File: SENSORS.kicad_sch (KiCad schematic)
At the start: 25 parts, among them J8 Conn_01x04, J9 Conn_01x04, U5 BMI088, U6 LSM6DSV16X, U7 ICM-45686, U8 BMP581, U9 DPS368XTSA1

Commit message: change package
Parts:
- U7: CAD Symbol Verification Pinout cross-checked against TDK DS-000577 Rev 1.0; Ultra L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 -> (none); DigiKey Description IMU ACCEL GYRO 6 AXIS -> (none); DigiKey Detailed Description Accelerometer, Gyroscope, 6 Axis Sensor I2C, I3C, SPI Output -> (none); DigiKey Digi-Reel Part Number 1428-ICM-45686DKR-ND -> (none); DigiKey ECCN EAR99 -> (none); DigiKey EDA Models URL https://www.digikey.com/en/models/24374985 -> (none); DigiKey HTSUS 8542.39.0070 -> (none); DigiKey MSL 1 (Unlimited) -> (none); DigiKey Mounting Surface Mount -> (none); DigiKey Package Case 14-VFLGA -> (none); DigiKey Part Status Active -> (none); DigiKey Price Qty 1 CT -> (none); DigiKey REACH Not Affected -> (none); DigiKey RoHS RoHS 3 Compliant -> (none); DigiKey Series SmartMotion -> (none); DigiKey Specs 6-axis accel + gyro, I2C/I3C/SPI, LGA-14 3.0x2.5 mm -> (none); DigiKey Standard Lead Time 45 Weeks -> (none); DigiKey Status Active; no stock at audit -> (none); DigiKey Stock 0 -> (none); DigiKey Supplier Device Package 14-LGA (2.5x3) -> (none); DigiKey TR Part Number 1428-ICM-45686TR-ND -> (none); DigiKey Unit Price EUR 4.60 -> (none); Footprint Audit Package dimensions confirmed from DigiKey/TDK; current foot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 -> (none); LCSC C22459454 -> (none); LCSC Part C22459454 -> (none); Library Audit Project-local H743_Ardupilot symbol; pinout from TDK datash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 -> (none); Price Checked 2026-09-25 -> (none)
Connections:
- net +3V3_MCU: now also U7.5 (VDDIO)
- net +3V3_SENS: now also U7.8 (VDD)
- net GND: now also U7.6 (GND)
- net SPI1.CS: now also U7.12 (CS)
- net SPI1.MISO: now also U7.1 (SDO/AD0)
- net SPI1.MOSI: now also U7.14 (SDI/SDIO/SDA)
- net SPI1.SCLK: now also U7.13 (SCLK/SCL)
- net at R28.2: now also U7.4 (INT1)
- net at R29.2: now also U7.9 (INT2/FSYNC/CLKIN)
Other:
- moved on the sheet: R28, R29

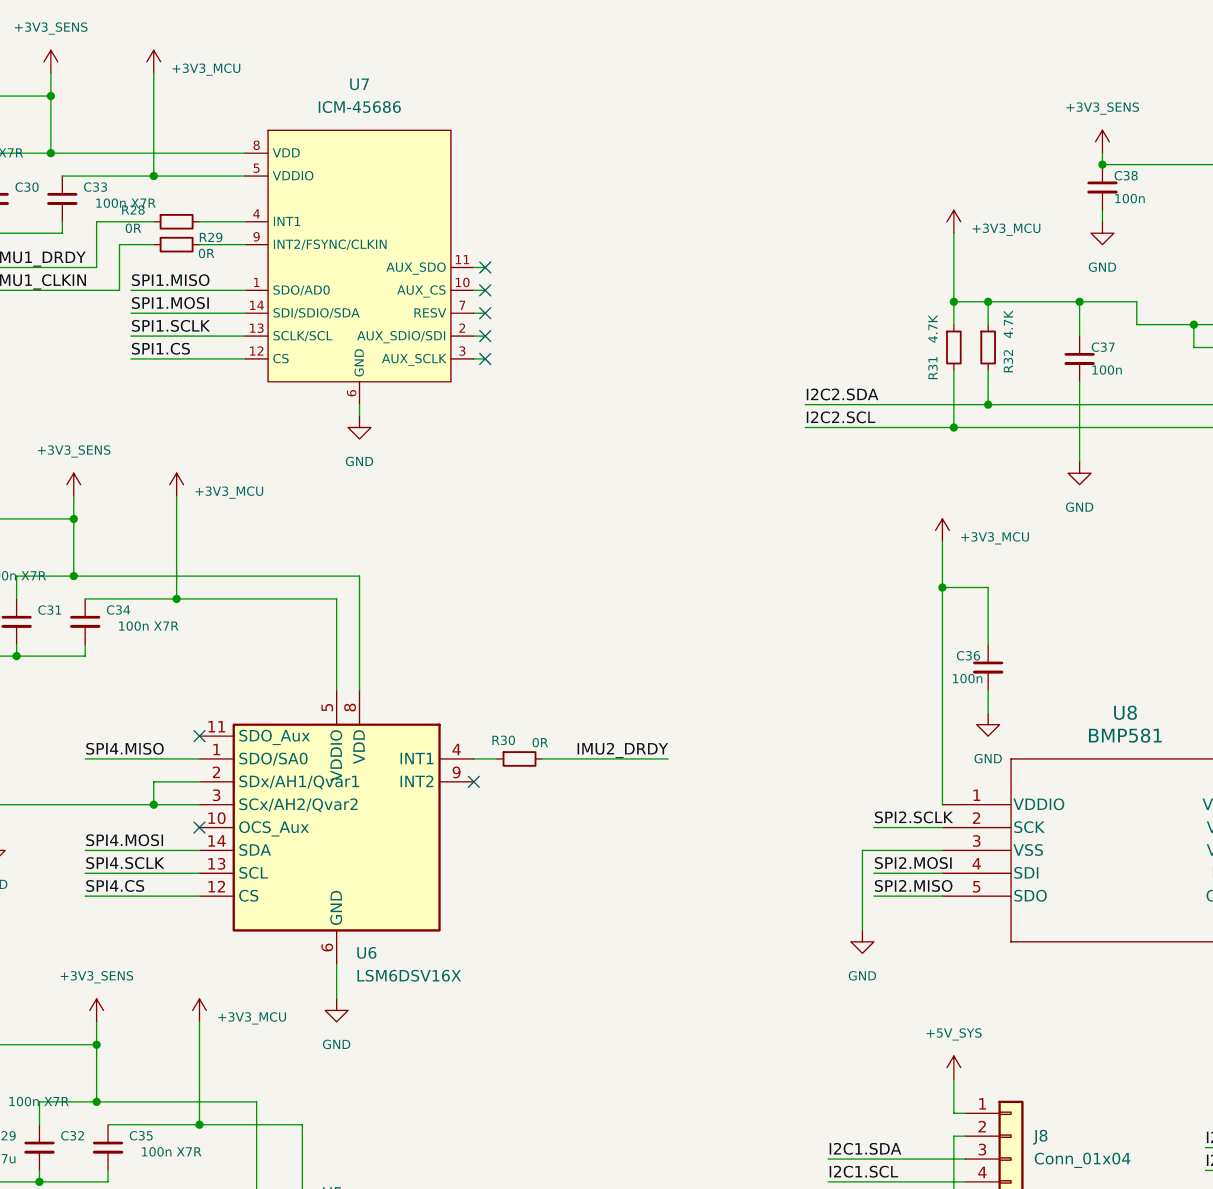
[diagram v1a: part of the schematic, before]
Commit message: move all sensor VDDIO rails to 3V3_SENS
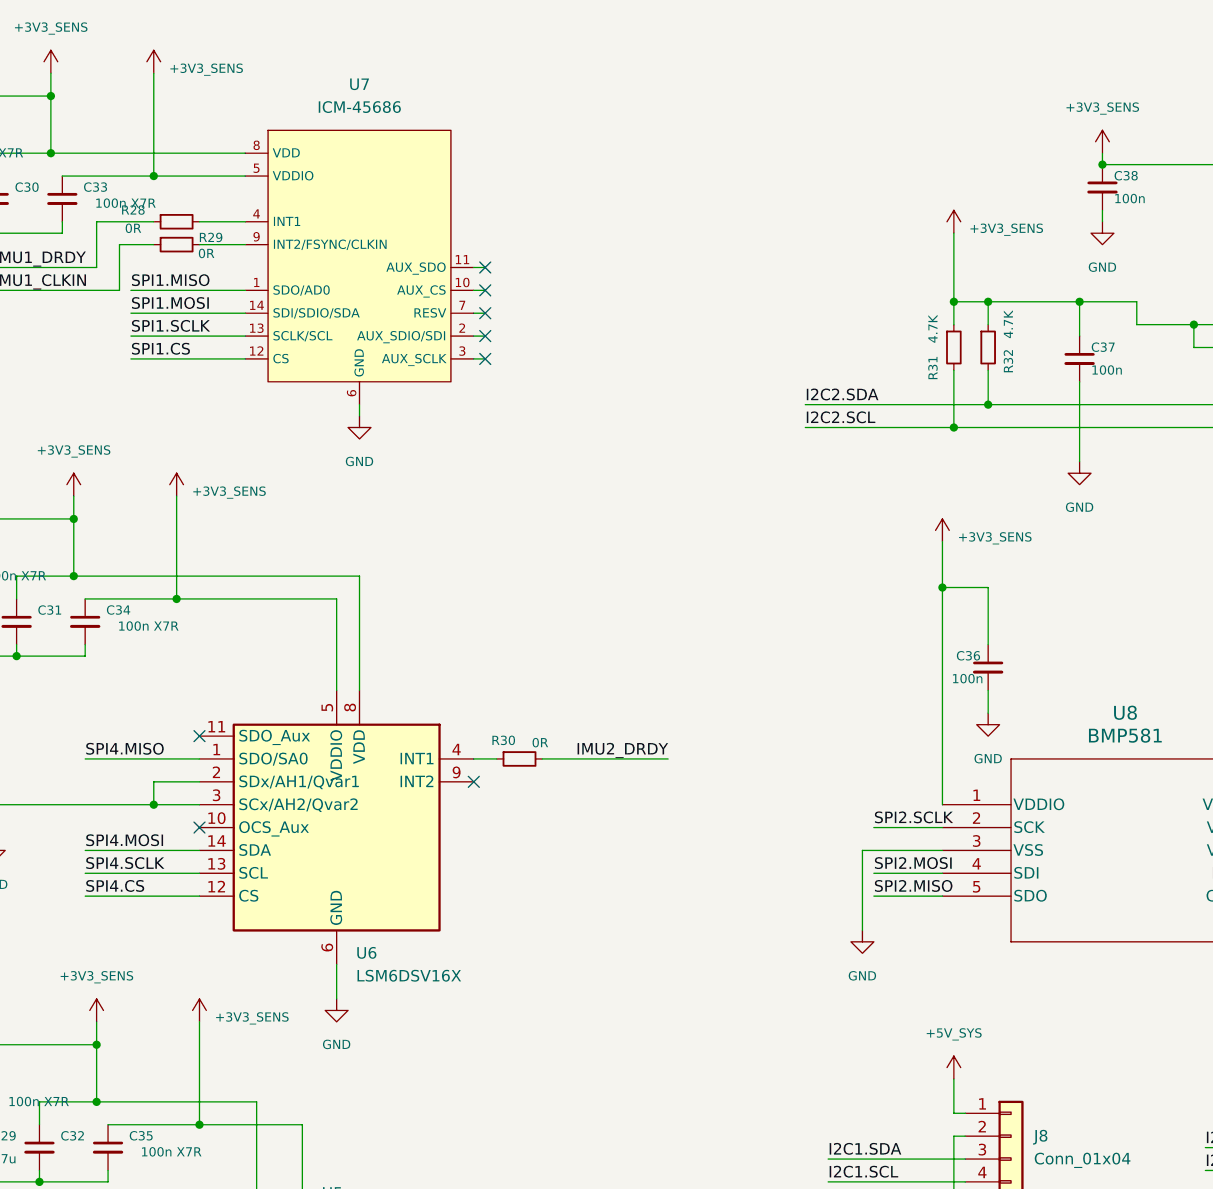
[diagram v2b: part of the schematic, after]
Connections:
- net +3V3_MCU is gone; now on net +3V3_SENS: C33.1, C34.1, C35.1, C36.1, C37.1, R31.1, R32.1, U5.11 (VDDIO), U6.5 (VDDIO), U7.5 (VDDIO), U8.1 (VDDIO), U9.2 (CSB), U9.6 (VDDIO)
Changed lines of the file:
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@@
 			)
 		)
-		(property "Value" "+3V3_MCU"
+		(property "Value" "+3V3_SENS"
 			(at 129.032 126.492 0)
 			(show_name no)
@@
 			)
 		)
-		(property "Value" "+3V3_MCU"
+		(property "Value" "+3V3_SENS"
 			(at 211.582 73.152 0)
 			(show_name no)
@@
 			)
 		)
-		(property "Value" "+3V3_MCU"
+		(property "Value" "+3V3_SENS"
 			(at 126.492 68.072 0)
 			(show_name no)
@@
 			)
 		)
-		(property "Value" "+3V3_MCU"
+		(property "Value" "+3V3_SENS"
 			(at 212.852 38.862 0)
 			(show_name no)
@@
 			)
 		)
-		(property "Value" "+3V3_MCU"
+		(property "Value" "+3V3_SENS"
 			(at 123.952 21.082 0)
 			(show_name no)

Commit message: restore sensor VDDIO rails to 3V3_MCU
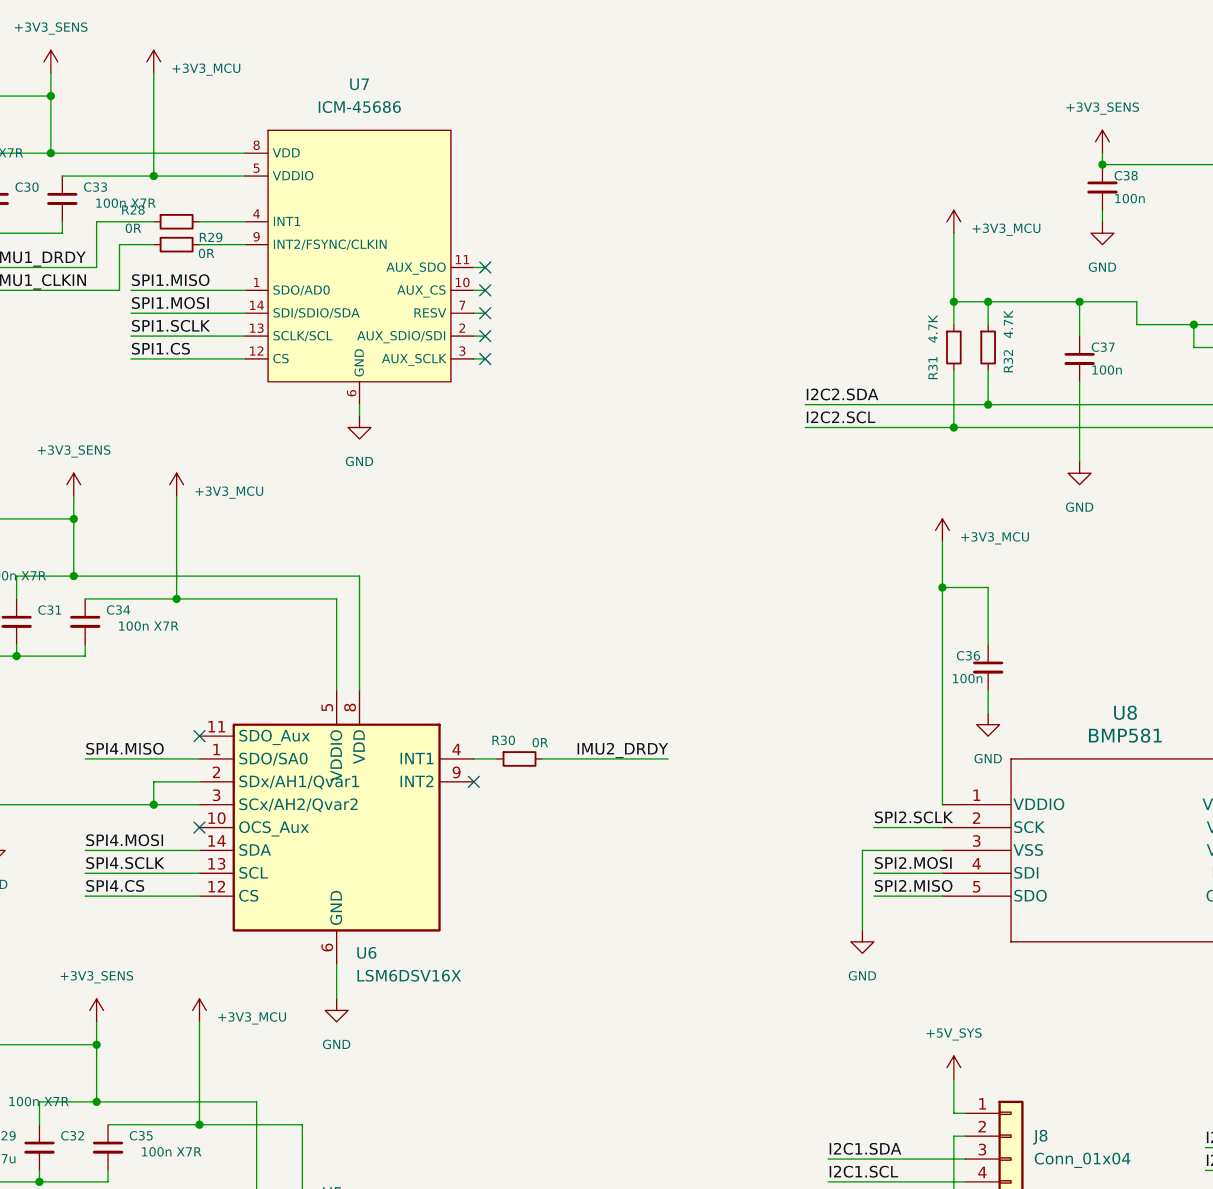
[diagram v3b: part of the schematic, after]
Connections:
- net +3V3_SENS: no longer C33.1, C34.1, C35.1, C36.1, C37.1, R31.1, R32.1, U5.11 (VDDIO), U6.5 (VDDIO), U7.5 (VDDIO), U8.1 (VDDIO), U9.2 (CSB), U9.6 (VDDIO)
- new net +3V3_MCU: C33.1, C34.1, C35.1, C36.1, C37.1, R31.1, R32.1, U5.11 (VDDIO), U6.5 (VDDIO), U7.5 (VDDIO), U8.1 (VDDIO), U9.2 (CSB), U9.6 (VDDIO)
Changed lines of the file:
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@@
 			)
 		)
-		(property "Value" "+3V3_SENS"
+		(property "Value" "+3V3_MCU"
 			(at 129.032 126.492 0)
 			(show_name no)
@@
 			)
 		)
-		(property "Value" "+3V3_SENS"
+		(property "Value" "+3V3_MCU"
 			(at 211.582 73.152 0)
 			(show_name no)
@@
 			)
 		)
-		(property "Value" "+3V3_SENS"
+		(property "Value" "+3V3_MCU"
 			(at 126.492 68.072 0)
 			(show_name no)
@@
 			)
 		)
-		(property "Value" "+3V3_SENS"
+		(property "Value" "+3V3_MCU"
 			(at 212.852 38.862 0)
 			(show_name no)
@@
 			)
 		)
-		(property "Value" "+3V3_SENS"
+		(property "Value" "+3V3_MCU"
 			(at 123.952 21.082 0)
 			(show_name no)

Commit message: assign Matek-style solder pad footprints in SENSORS.kicad_sch
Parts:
- J8, J9: footprint (none) -> H743_Custom:SolderPadArray_1x04_P2.54mm_1x1mm; DigiKey Status TBD: connector not physically selected -> PCB feature / no purchased component; Footprint Audit BLOCKING: no footprint assigned -> OK: 4 square SMD pads 1.00x1.00 mm, P2.54 mm, no holes, no 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; Library Audit Generic KiCad connector -> Project-local H743_Custom footprint; Package TBD -> Solder pad array 1x4, P2.54 mm, 1.00x1.00 mm SMD
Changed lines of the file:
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@@
 			)
 		)
-		(property "Footprint" ""
+		(property "Footprint" "H743_Custom:SolderPadArray_1x04_P2.54mm_1x1mm"
 			(at 255.27 138.43 0)
 			(hide yes)
@@
 			)
 		)
-		(property "DigiKey Status" "TBD: connector not physically selected"
+		(property "DigiKey Status" "PCB feature / no purchased component"
 			(at 257.81 138.4299 0)
 			(hide yes)
@@
 			)
 		)
-		(property "Package" "TBD"
+		(property "Package" "Solder pad array 1x4, P2.54 mm, 1.00x1.00 mm SMD"
 			(at 257.81 138.4299 0)
 			(hide yes)
@@
 			)
 		)
-		(property "Footprint Audit" "BLOCKING: no footprint assigned"
+		(property "Footprint Audit" "OK: 4 square SMD pads 1.00x1.00 mm, P2.54 mm, no holes, no paste"
 			(at 257.81 138.4299 0)
 			(hide yes)
@@
 			)
 		)
-		(property "Library Audit" "Generic KiCad connector"
+		(property "Library Audit" "Project-local H743_Custom footprint"
 			(at 257.81 138.4299 0)
 			(hide yes)
@@
 			)
 		)
-		(property "Footprint" ""
+		(property "Footprint" "H743_Custom:SolderPadArray_1x04_P2.54mm_1x1mm"
 			(at 213.36 139.7 0)
 			(hide yes)
@@
 			)
 		)
-		(property "DigiKey Status" "TBD: connector not physically selected"
+		(property "DigiKey Status" "PCB feature / no purchased component"
 			(at 215.9 139.6999 0)
 			(hide yes)
@@
 			)
 		)
-		(property "Package" "TBD"
+		(property "Package" "Solder pad array 1x4, P2.54 mm, 1.00x1.00 mm SMD"
 			(at 215.9 139.6999 0)
 			(hide yes)
@@
 			)
 		)
-		(property "Footprint Audit" "BLOCKING: no footprint assigned"
+		(property "Footprint Audit" "OK: 4 square SMD pads 1.00x1.00 mm, P2.54 mm, no holes, no paste"
 			(at 215.9 139.6999 0)
 			(hide yes)
@@
 			)
 		)
-		(property "Library Audit" "Generic KiCad connector"
+		(property "Library Audit" "Project-local H743_Custom footprint"
 			(at 215.9 139.6999 0)
 			(hide yes)

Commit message: update
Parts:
- renumbered C27 to C44, C28 to C45, C29 to C46, C30 to C47, C31 to C48, C32 to C49, C33 to C50, C34 to C51, C35 to C52, C36 to C53, C37 to C54, C38 to C55, C39 to C56, R28 to R34, R29 to R35, R30 to R36, R31 to R37, R32 to R38, U6 to U10, U7 to U11, U8 to U12, U9 to U13, U5 to U9

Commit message: update pcb
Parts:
- J8: value Conn_01x04 -> I2C1
- J9: value Conn_01x04 -> I2C_2
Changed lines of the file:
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@@
 			)
 		)
-		(property "Value" "Conn_01x04"
+		(property "Value" "I2C_2"
 			(at 257.81 140.9699 0)
 			(show_name no)
@@
 			)
 		)
-		(property "Value" "Conn_01x04"
+		(property "Value" "I2C1"
 			(at 215.9 142.2399 0)
 			(show_name no)

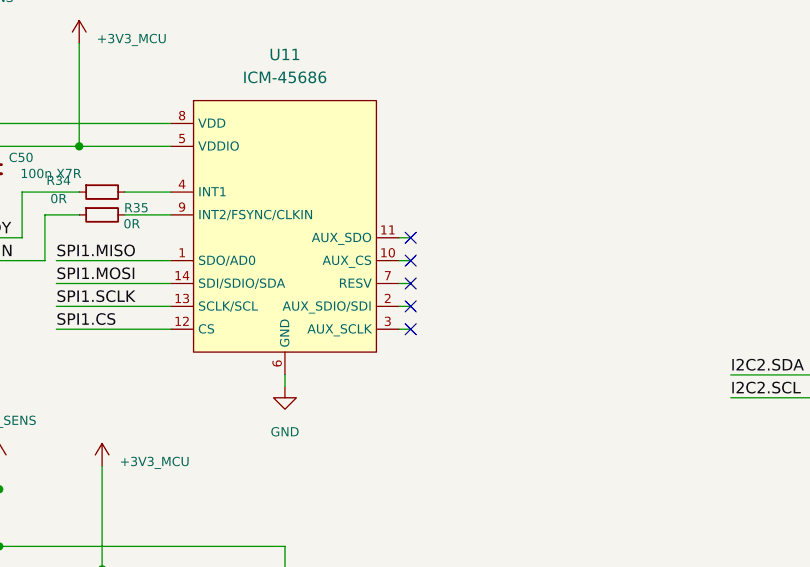
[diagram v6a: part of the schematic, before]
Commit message: Review component footprints, restore local libraries and reconcile PCB pads
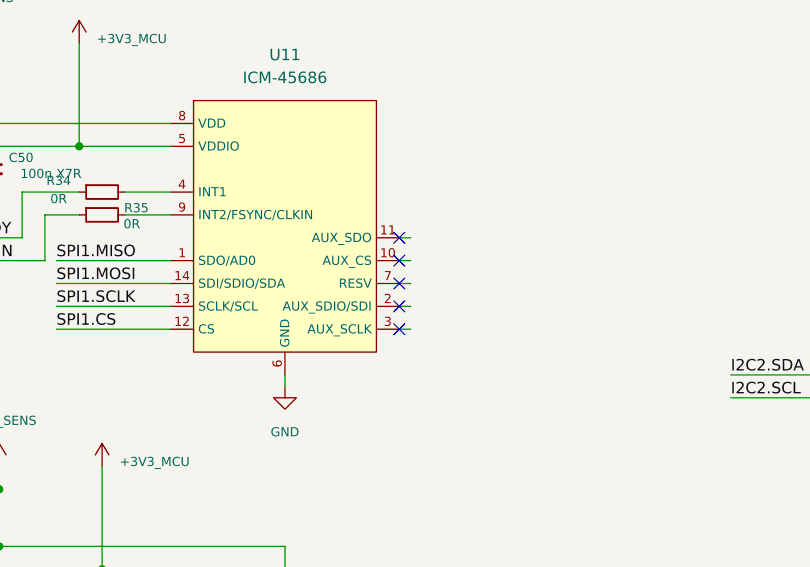
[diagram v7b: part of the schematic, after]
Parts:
- C44, C45, C46, C47, C48, C49, C50, C51, C52, C53, C54, C55, C56: symbol Device:C_Small -> FC01_Project:SENSORS__C_Small; Footprint Audit OK -> See verification/COMPONENTS.csv and verification/REPORT.md; Library Audit KiCad standard -> See verification/COMPONENTS.csv and verification/REPORT.md
- J8, J9: symbol Connector_Generic:Conn_01x04 -> FC01_Project:SENSORS__Conn_01x04; Footprint Audit OK: 4 square SMD pads 1.00x1.00 mm, P2.54 mm, no holes, no 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 -> See verification/COMPONENTS.csv and verification/REPORT.md; Library Audit Project-local H743_Custom footprint -> See verification/COMPONENTS.csv and verification/REPORT.md
- R34, R35, R36, R37, R38: symbol Device:R_Small -> FC01_Project:SENSORS__R_Small; Footprint Audit OK -> See verification/COMPONENTS.csv and verification/REPORT.md; Library Audit KiCad standard -> See verification/COMPONENTS.csv and verification/REPORT.md
- U10: symbol H743_Ardupilot:LSM6DSV16X -> FC01_Project:SENSORS__LSM6DSV16X; Footprint Audit OK: KiCad LGA-14 3x2.5 P0.5 -> See verification/COMPONENTS.csv and verification/REPORT.md; Library Audit Embedded H743_Ardupilot symbol + KiCad footprint -> See verification/COMPONENTS.csv and verification/REPORT.md
- U11: footprint EasyEDA:LGA-14_L3.0-W2.5-P0.50-TL -> H743_Custom:TDK_ICM45686_LGA14_3x2.5mm; symbol H743_Ardupilot:ICM-45686 -> FC01_Project:SENSORS__ICM-45686
- U12: symbol BMP581:BMP581 -> FC01_Project:SENSORS__BMP581; Footprint Audit OK: Bosch recommended land pattern corrected 2026-09-25 -> See verification/COMPONENTS.csv and verification/REPORT.md; Library Audit Project BMP581 symbol + H743_Custom footprint -> See verification/COMPONENTS.csv and verification/REPORT.md
- U13: footprint EasyEDA:LGA-8_L2.5-W2.0-P0.65-TR_DPS368 -> H743_Custom:Infineon_DPS368_PG-VLGA-8-2; symbol EasyEDA:DPS368XTSA1 -> FC01_Project:SENSORS__DPS368XTSA1_1; Footprint Audit OK by dimensions; final land-pattern overlay recommended -> See verification/COMPONENTS.csv and verification/REPORT.md; Library Audit EasyEDA external -> See verification/COMPONENTS.csv and verification/REPORT.md
- U9: symbol Sensor_Motion:BMI088 -> FC01_Project:SENSORS__BMI088; Footprint Audit OK: KiCad Bosch LGA-16 -> See verification/COMPONENTS.csv and verification/REPORT.md; Library Audit KiCad Sensor_Motion -> See verification/COMPONENTS.csv and verification/REPORT.md
